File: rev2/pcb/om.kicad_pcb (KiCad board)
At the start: 2 copper layers, 137 x 108.8 mm, 32 parts, among them J1 Jumper

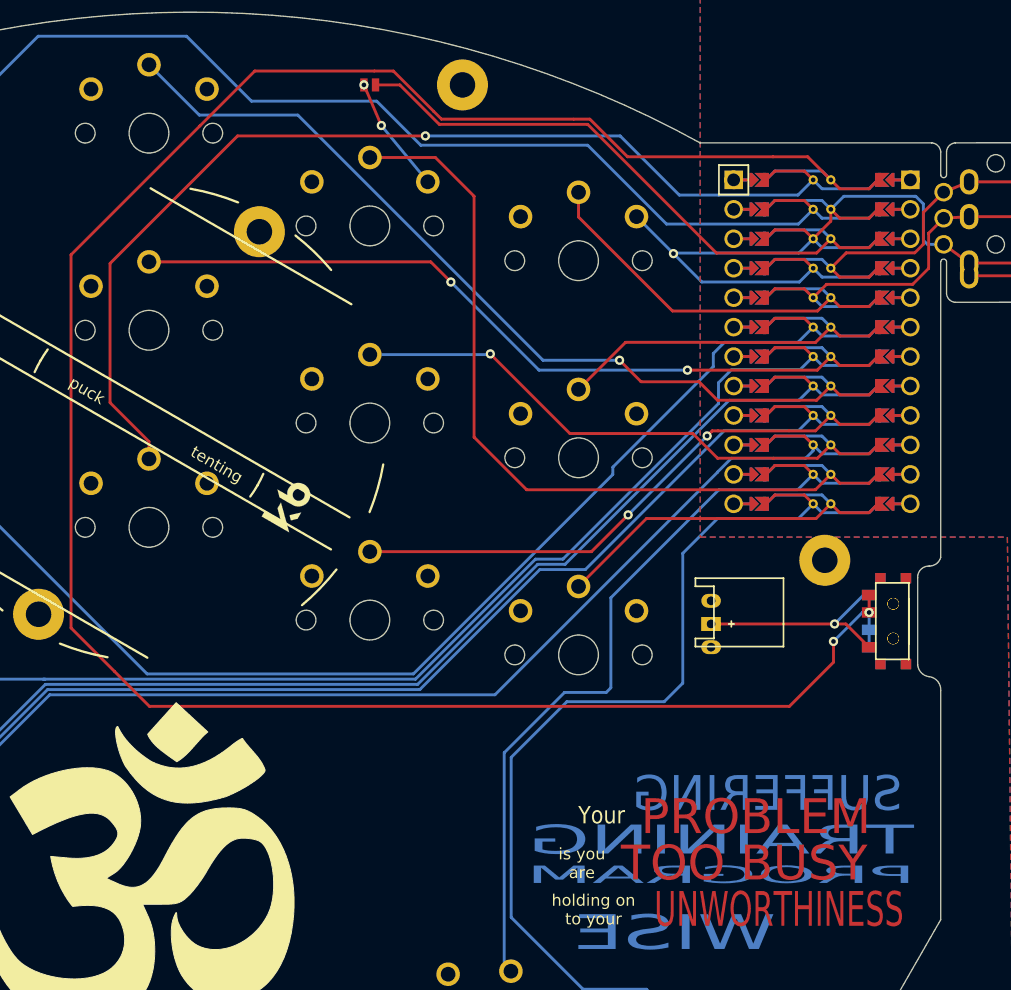
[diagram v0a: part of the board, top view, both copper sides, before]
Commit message: Fix rev2 cutouts for on / off, add througholes for MCU cover, choc mini now has reversible mini footprints
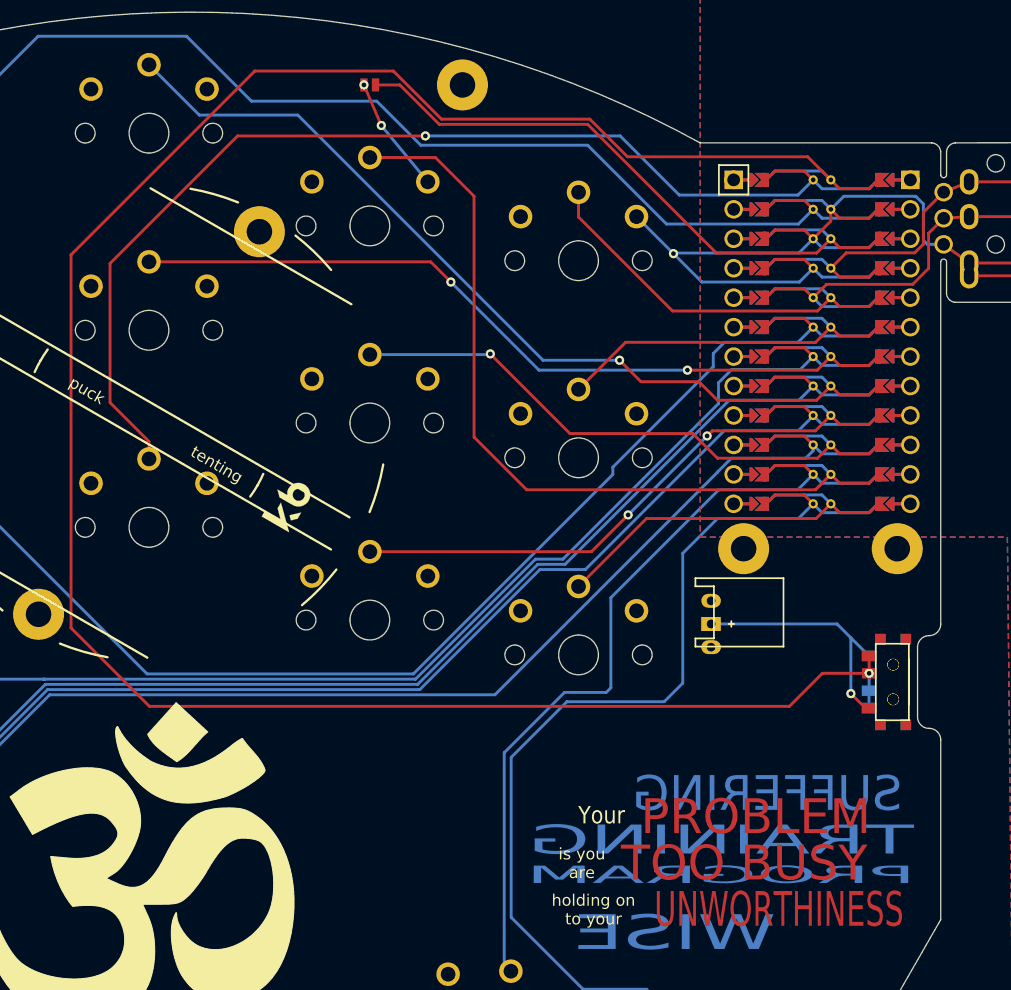
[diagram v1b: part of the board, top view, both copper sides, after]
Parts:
- added ?: , , F.Cu at (262.7, 145.5)
- moved ? 7.07 mm to (249.4, 145.5)
- moved T1 5.25 mm to (262.3, 157.0) (x2)
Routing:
- net RAW: track 188.7 -> 185.5 mm, vias 2 -> 1
- net POSITIVE: track 18.5 -> 21.7 mm
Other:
- outline, holes or cut-outs redrawn
